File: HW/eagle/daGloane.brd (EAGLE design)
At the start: 100 x 80 mm, 83 parts, among them IC1 MCP1252-33X50, U1 STM32F10XTXU6, X2 SPARKFUN-CONNECTORS_USB-MICROB

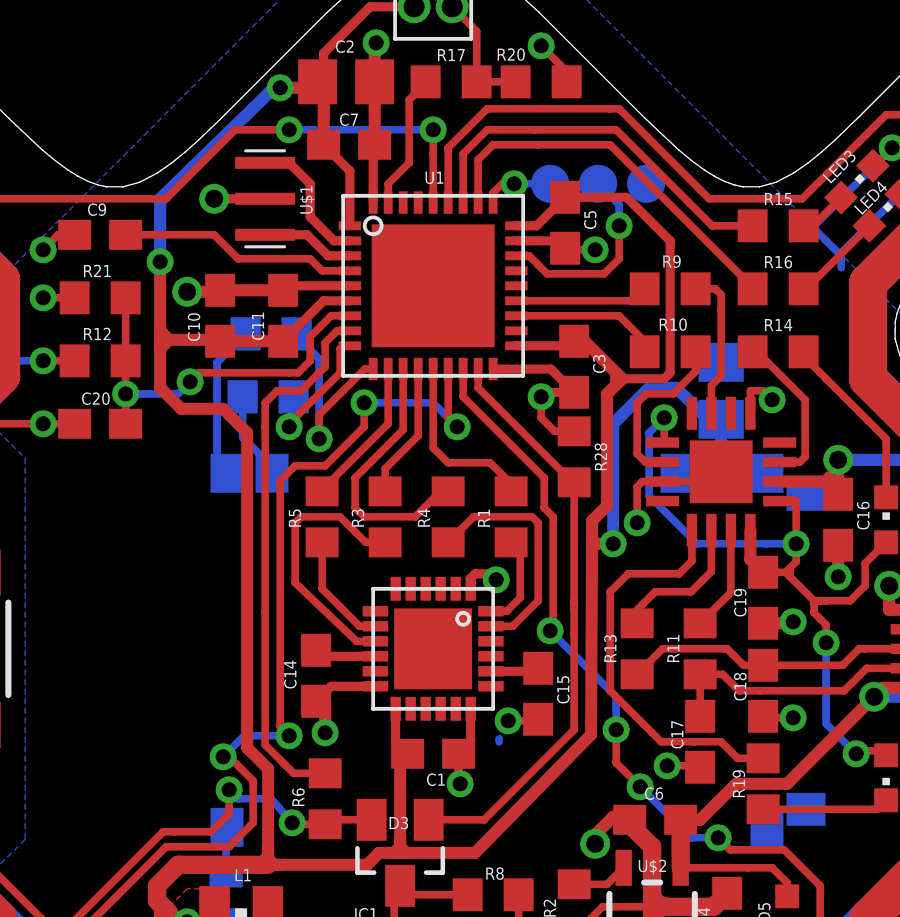
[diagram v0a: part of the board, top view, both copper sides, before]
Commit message: error in schematic fixed: Wrong pin of MPU6000 connected to GND
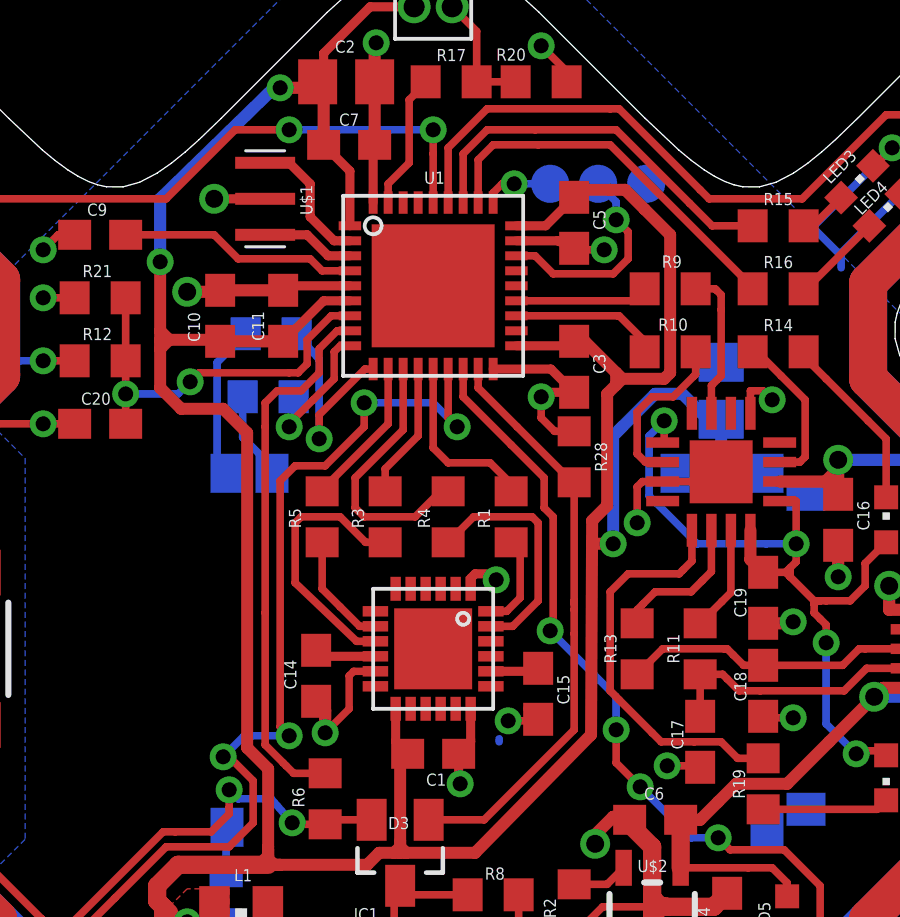
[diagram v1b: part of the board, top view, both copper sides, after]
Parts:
- moved C5 0.30 mm to (45.2, 54.7)
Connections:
- net GND: now also U$3.11; no longer U$3.12
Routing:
- net GND: track 84.2 -> 85.9 mm

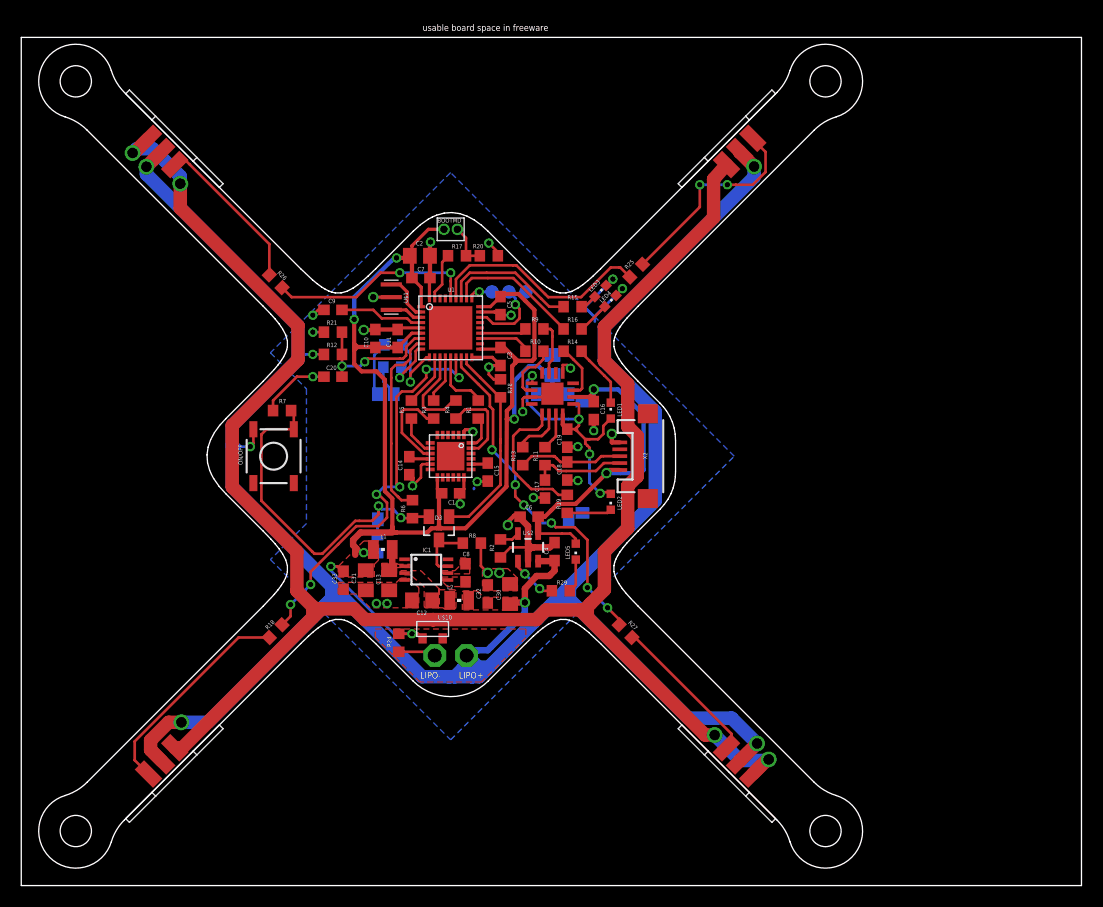
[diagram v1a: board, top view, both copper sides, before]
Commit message: - micro usb connector with electrical connection to mounting pad added - micro usb connector replaced with new part - micro usb connectors mounting pads' size increased with shape. This is to increase mechanical strength
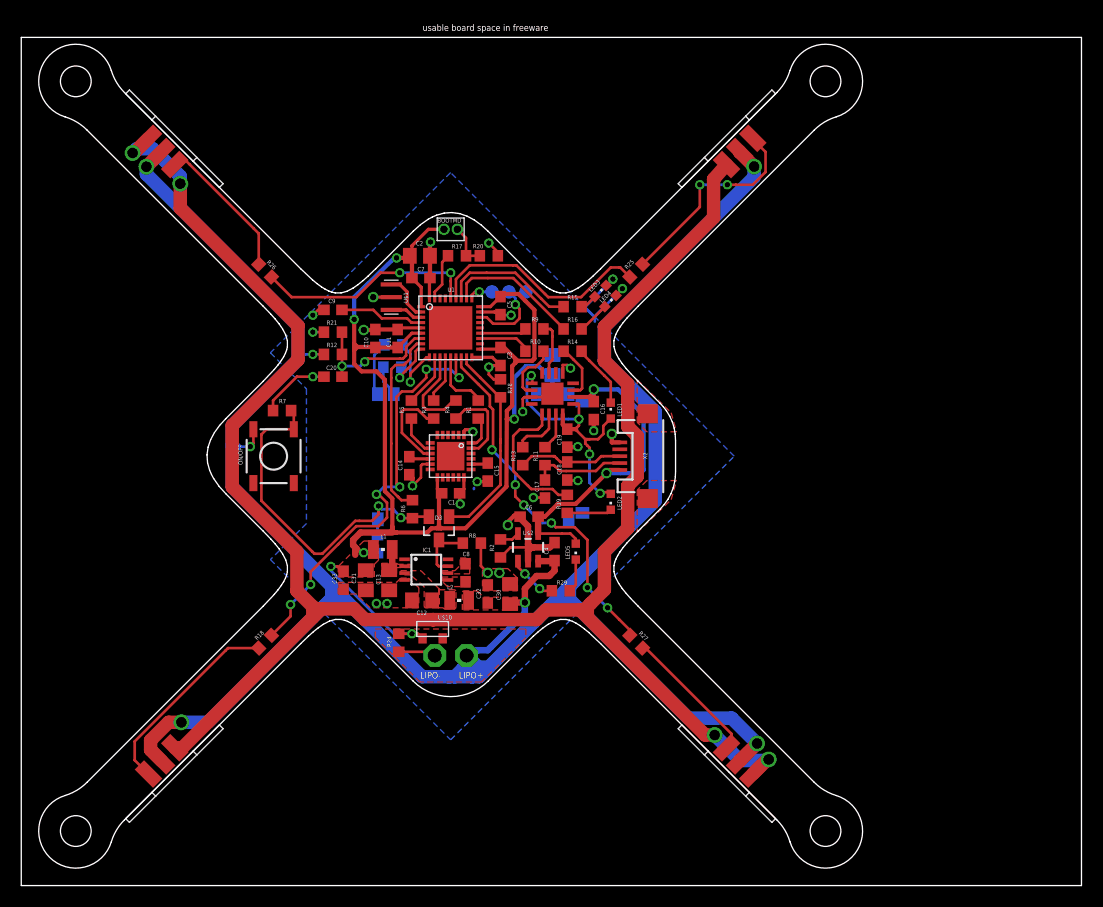
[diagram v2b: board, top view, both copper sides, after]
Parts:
- X2: value SPARKFUN-CONNECTORS_USB-MICROB -> USB_MICROB_PLUG_MT
- moved R18 1.41 mm to (23.0, 23.0)
- moved R26 1.41 mm to (23.0, 58.0)
- moved R27 1.41 mm to (58.0, 23.0)
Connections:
- new net MT_PAD1: X2.MT1
- new net MT_PAD2: X2.MT2
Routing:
- net N$41: track 15.5 -> 14.1 mm
- net N$39: track 14.7 -> 13.3 mm
- net N$22: track 20.4 -> 19.0 mm
- net MOT4: track 19.6 -> 21.1 mm
- net MOT1: track 39.1 -> 40.5 mm
- net MOT2: track 33.1 -> 34.5 mm
- added copper zone on layer 1, net MT_PAD1
- added copper zone on layer 1, net MT_PAD2

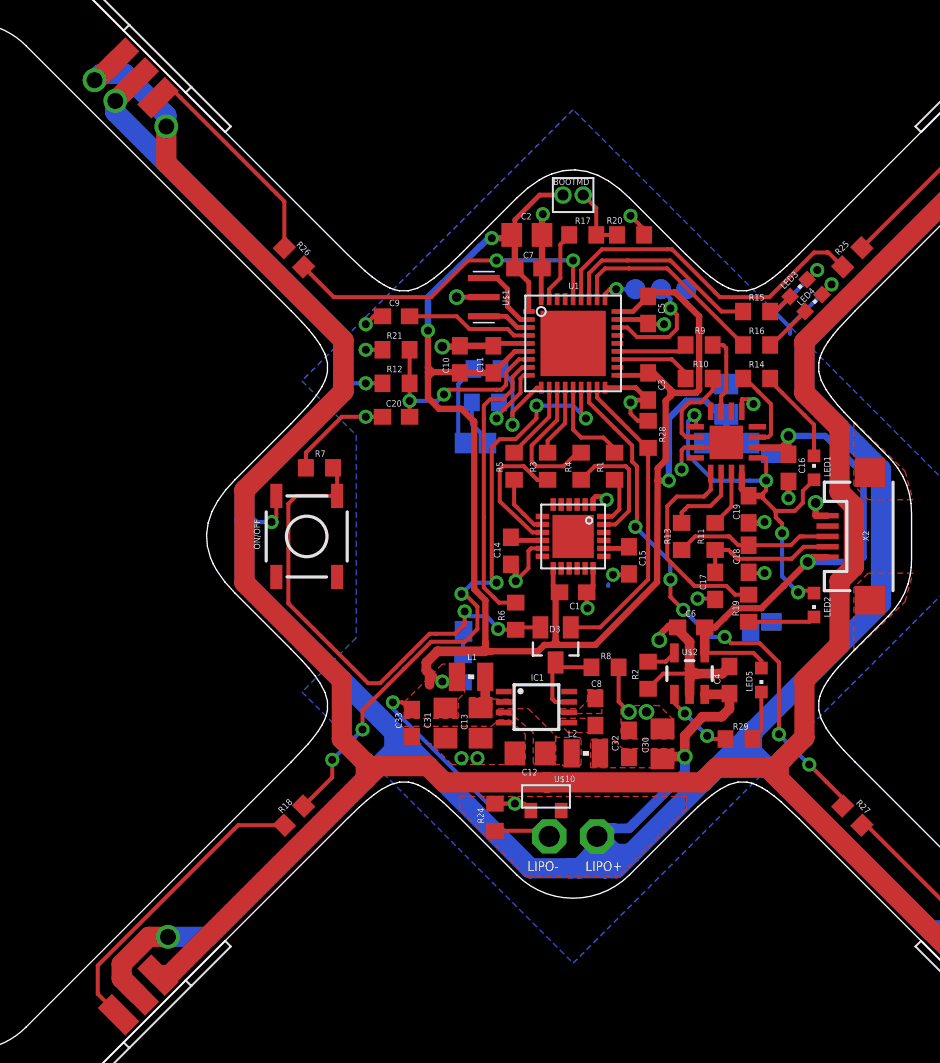
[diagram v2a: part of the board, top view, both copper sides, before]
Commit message: hole diameter for mounting of the motors changed. 2.95mm to 2.90mm
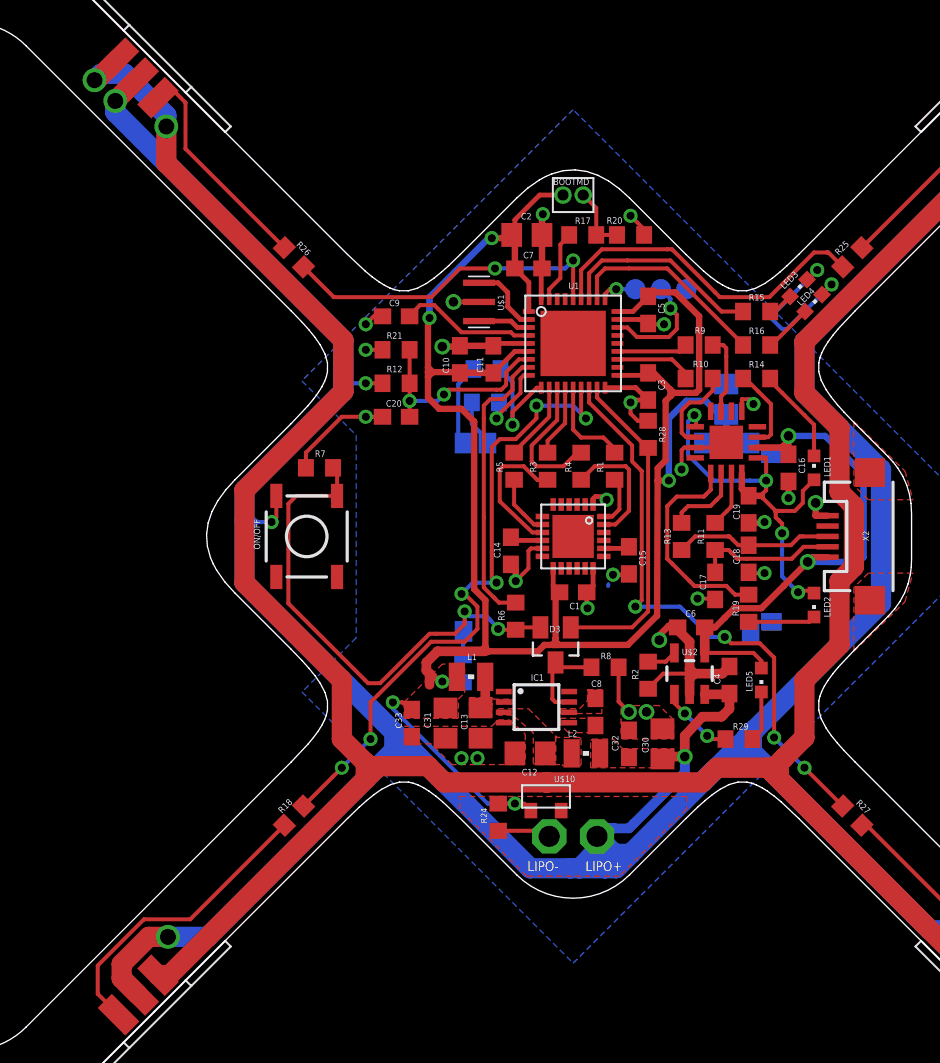
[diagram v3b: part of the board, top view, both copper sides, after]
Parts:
- moved U$1 0.42 mm to (34.6, 55.2)
- moved R24 0.20 mm to (35.8, 22.9)
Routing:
- net MOT2: track 34.5 -> 36.4 mm, vias 6 -> 4
- net PWR_ON_µC: track 19.5 -> 20.6 mm
- net VCC: track 131.0 -> 132.0 mm
- net GND: track 85.9 -> 85.2 mm
- net RESET1: track 7.97 -> 8.58 mm

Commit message: logo placed on pcb
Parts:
- added U$11: (no value), daGloane:DAGLOANE_LOGO
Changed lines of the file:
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@@
 <layer number="151" name="HeatSink" color="7" fill="1" visible="no" active="yes"/>
 <layer number="199" name="L$199" color="7" fill="1" visible="no" active="yes"/>
-<layer number="200" name="200bmp" color="15" fill="10" visible="no" active="yes"/>
+<layer number="200" name="200bmp" color="10" fill="10" visible="yes" active="yes"/>
 <layer number="201" name="201bmp" color="15" fill="10" visible="yes" active="yes"/>
 <layer number="202" name="202bmp" color="15" fill="10" visible="no" active="yes"/>
@@
 <element name="U$8" library="daGloane" package="3A_BLDC_CONTROLLER" value="3A_BLDC_CONTROLLER" x="68.5" y="68.5" rot="R135"/>
 <element name="U$9" library="daGloane" package="3A_BLDC_CONTROLLER" value="3A_BLDC_CONTROLLER" x="12.5" y="68.5" rot="R45"/>
+<element name="U$11" library="daGloane" package="DAGLOANE_LOGO" value="" x="30.5" y="40.5" rot="R90"/>
 </elements>
 <signals>

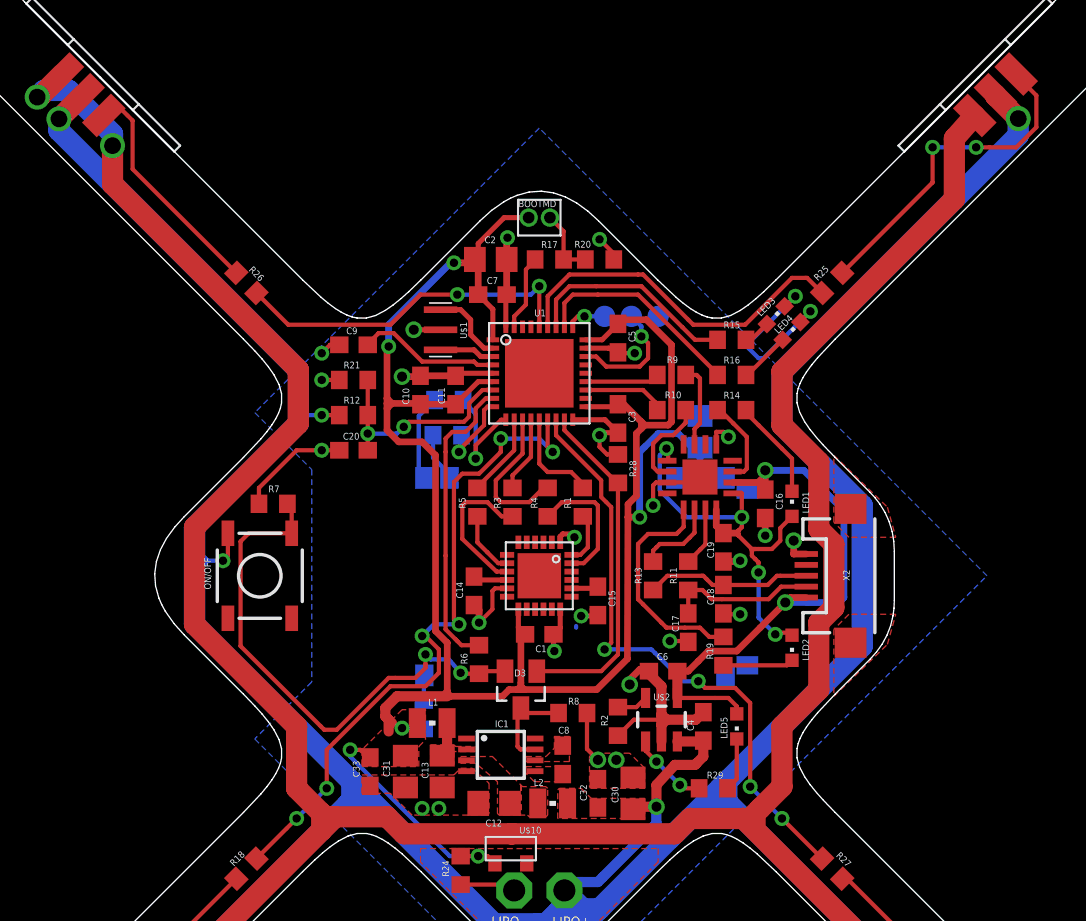
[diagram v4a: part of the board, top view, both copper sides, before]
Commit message: trace angles fixed
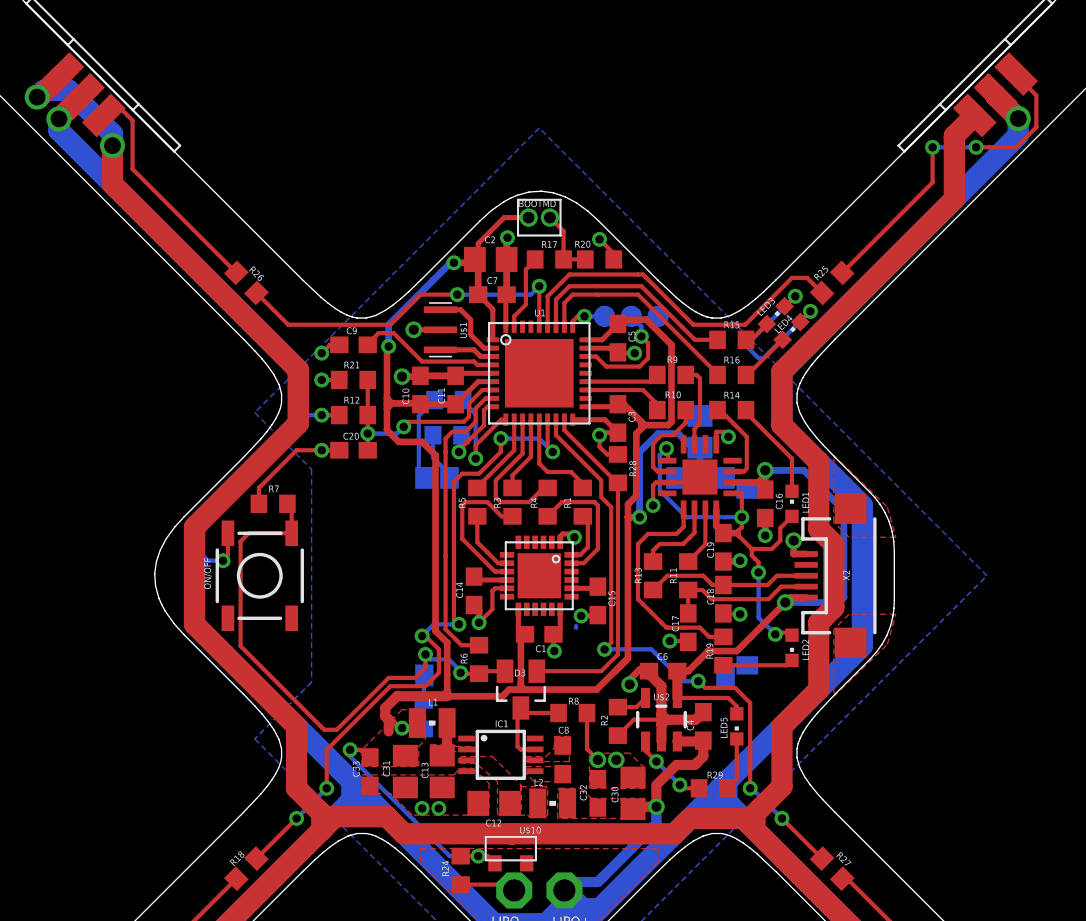
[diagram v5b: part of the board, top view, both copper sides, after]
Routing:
- net VCC: track 132.0 -> 133.4 mm
